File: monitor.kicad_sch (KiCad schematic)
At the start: 6 parts, among them K2 RT314A03, SW1 SW_Push, SW2 SW_Wuerth_450301014042, U2 LM397

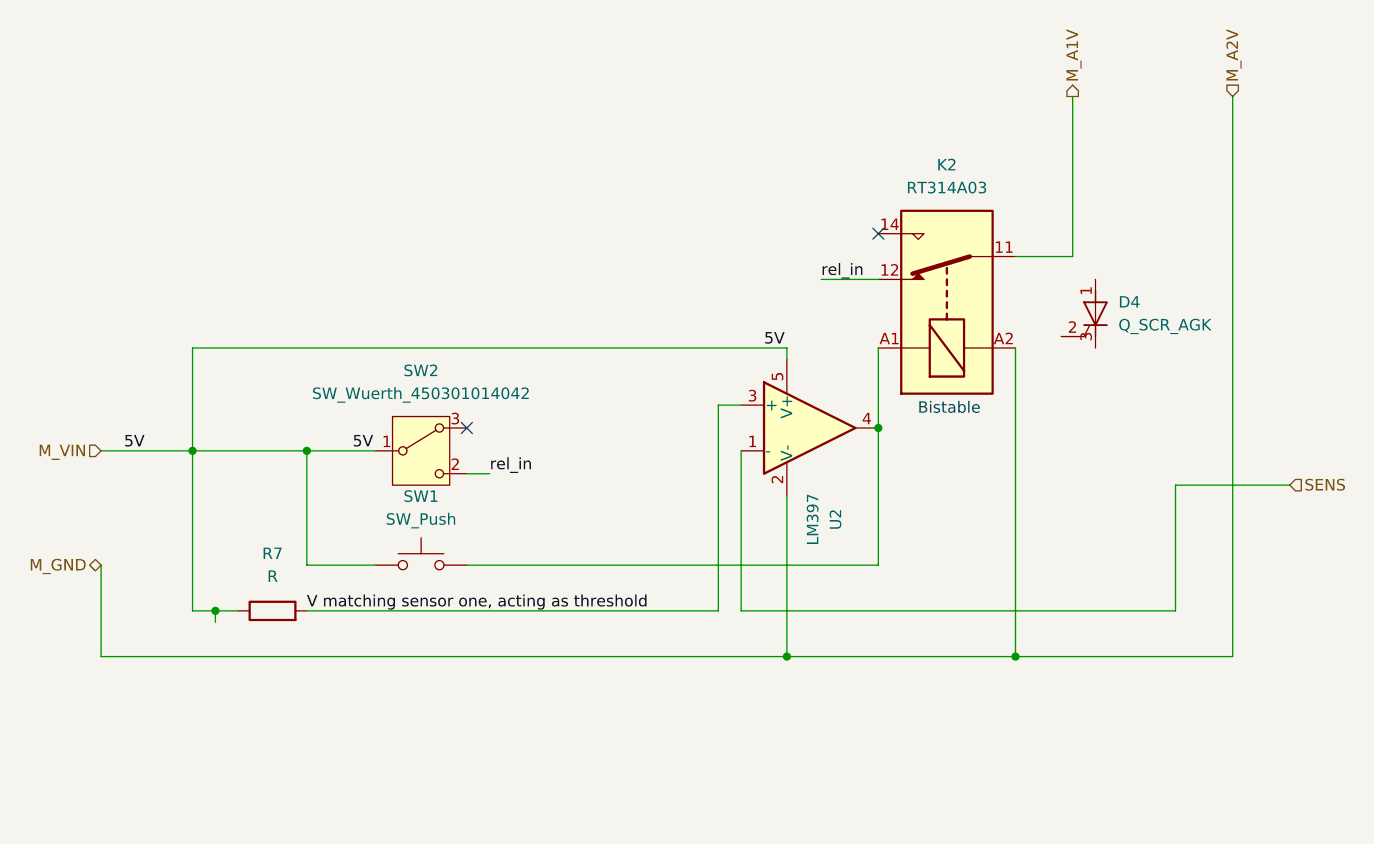
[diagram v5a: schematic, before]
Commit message: added scr instead of button
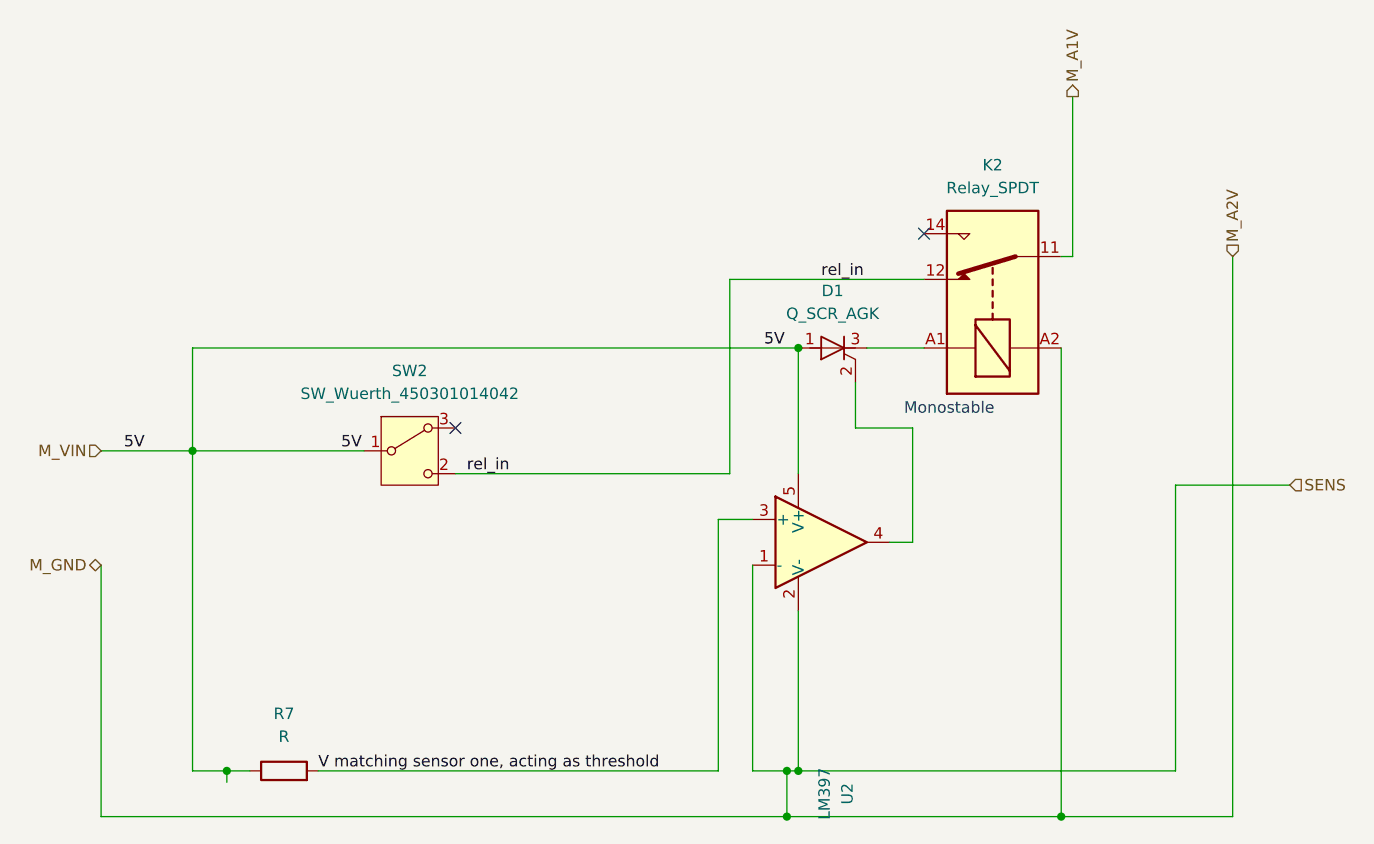
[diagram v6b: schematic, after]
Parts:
- removed D4: Q_SCR_AGK, symbol Device:Q_SCR_AGK
- removed K2: RT314A03, Relay_THT:Relay_SPDT_Schrack-RT1-16A-FormC_RM5mm, symbol Relay:RT314A05
- removed SW1: SW_Push, symbol Switch:SW_Push
- added D1: Q_SCR_AGK, symbol Device:Q_SCR_AGK
- added K2: Relay_SPDT, symbol Relay:Relay_SPDT
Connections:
- net SENS is gone; now on net M_A2V: U2.1 (-)
- net M_A1V: now also K2.11
- net M_A2V: now also K2.A2
- net M_VIN: now also D1.1 (A)
- net rel_in: now also K2.12
- net at U2.4: now also D1.2 (G)
- new net: D1.3 (K), K2.A1
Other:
- note added: "Monostable"
- note removed: "Bistable"
- moved on the sheet: R7, SW2, U2

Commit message: comparator wirirng
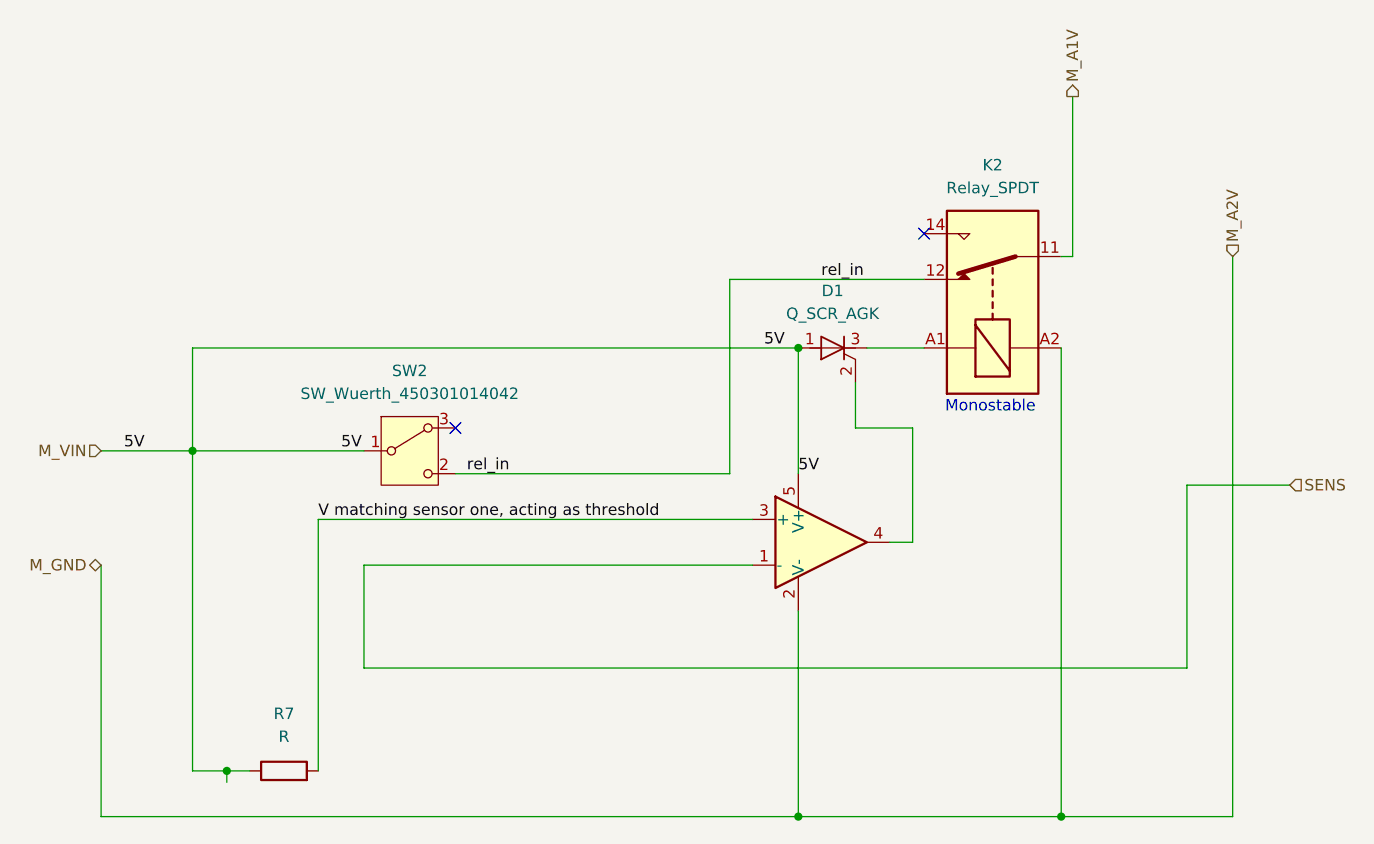
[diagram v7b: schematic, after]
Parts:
- K2: footprint (none) -> Relay_THT:Relay_SPDT_Finder_32.21-x000
- R7: footprint (none) -> Resistor_SMD:R_0201_0603Metric
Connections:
- net M_A2V: no longer U2.1 (-)
- new net SENS: U2.1 (-)
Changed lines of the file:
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@@
 	(text "Monostable"
 		(exclude_from_sim no)
-		(at 169.164 76.708 0)
+		(at 173.736 76.454 0)
 		(effects
 			(font
@@
 	)
 	(junction
-		(at 88.9 116.84)
+		(at 152.4 121.92)
 		(diameter 0)
 		(color 0 0 0 0)
 	)
 	(junction
-		(at 151.13 116.84)
+		(at 88.9 116.84)
 		(diameter 0)
 		(color 0 0 0 0)
@@
 	)
 	(junction
-		(at 152.4 116.84)
-		(diameter 0)
-		(color 0 0 0 0)
-	)
-	(junction
-		(at 151.13 121.92)
-		(diameter 0)
-		(color 0 0 0 0)
-	)
-	(junction
 		(at 85.09 81.28)
 		(diameter 0)
@@
 	(wire
 		(pts
-			(xy 151.13 116.84) (xy 147.32 116.84)
-		)
-		(stroke
-			(width 0)
-			(type default)
-		)
-	)
-	(wire
-		(pts
-			(xy 74.93 121.92) (xy 151.13 121.92)
-		)
-		(stroke
-			(width 0)
-			(type default)
-		)
-	)
-	(wire
-		(pts
-			(xy 143.51 88.9) (xy 143.51 116.84)
-		)
-		(stroke
-			(width 0)
-			(type default)
-		)
-	)
-	(wire
-		(pts
-			(xy 152.4 116.84) (xy 151.13 116.84)
+			(xy 74.93 121.92) (xy 152.4 121.92)
+		)
+		(stroke
+			(width 0)
+			(type default)
+		)
+	)
+	(wire
+		(pts
+			(xy 104.14 93.98) (xy 147.32 93.98)
 		)
 		(stroke
@@
 	(wire
 		(pts
+			(xy 99.06 88.9) (xy 99.06 116.84)
+		)
+		(stroke
+			(width 0)
+			(type default)
+		)
+	)
+	(wire
+		(pts
 			(xy 85.09 69.85) (xy 152.4 69.85)
 		)
@@
 	(wire
 		(pts
-			(xy 152.4 83.82) (xy 152.4 69.85)
+			(xy 152.4 69.85) (xy 152.4 83.82)
 		)
 		(stroke
@@
 	(wire
 		(pts
+			(xy 104.14 93.98) (xy 104.14 105.41)
+		)
+		(stroke
+			(width 0)
+			(type default)
+		)
+	)
+	(wire
+		(pts
 			(xy 144.78 62.23) (xy 166.37 62.23)
 		)
@@
 	(wire
 		(pts
+			(xy 152.4 121.92) (xy 181.61 121.92)
+		)
+		(stroke
+			(width 0)
+			(type default)
+		)
+	)
+	(wire
+		(pts
 			(xy 114.3 83.82) (xy 144.78 83.82)
 		)
@@
 	(wire
 		(pts
-			(xy 152.4 99.06) (xy 152.4 116.84)
+			(xy 152.4 99.06) (xy 152.4 121.92)
 		)
 		(stroke
@@
 	(wire
 		(pts
-			(xy 151.13 121.92) (xy 181.61 121.92)
-		)
-		(stroke
-			(width 0)
-			(type default)
-		)
-	)
-	(wire
-		(pts
 			(xy 200.66 121.92) (xy 200.66 59.69)
 		)
@@
 	(wire
 		(pts
-			(xy 147.32 116.84) (xy 147.32 93.98)
-		)
-		(stroke
-			(width 0)
-			(type default)
-		)
-	)
-	(wire
-		(pts
 			(xy 165.1 91.44) (xy 165.1 78.74)
 		)
@@
 	(wire
 		(pts
-			(xy 194.31 116.84) (xy 152.4 116.84)
-		)
-		(stroke
-			(width 0)
-			(type default)
-		)
-	)
-	(wire
-		(pts
-			(xy 151.13 116.84) (xy 151.13 121.92)
-		)
-		(stroke
-			(width 0)
-			(type default)
-		)
-	)
-	(wire
-		(pts
-			(xy 194.31 85.09) (xy 194.31 116.84)
-		)
-		(stroke
-			(width 0)
-			(type default)
-		)
-	)
-	(wire
-		(pts
-			(xy 207.01 85.09) (xy 194.31 85.09)
-		)
-		(stroke
-			(width 0)
-			(type default)
-		)
-	)
-	(wire
-		(pts
-			(xy 99.06 116.84) (xy 143.51 116.84)
+			(xy 104.14 105.41) (xy 195.58 105.41)
+		)
+		(stroke
+			(width 0)
+			(type default)
+		)
+	)
+	(wire
+		(pts
+			(xy 195.58 85.09) (xy 195.58 105.41)
+		)
+		(stroke
+			(width 0)
+			(type default)
+		)
+	)
+	(wire
+		(pts
+			(xy 207.01 85.09) (xy 195.58 85.09)
+		)
+		(stroke
+			(width 0)
+			(type default)
+		)
+	)
+	(wire
+		(pts
+			(xy 99.06 88.9) (xy 147.32 88.9)
 		)
 		(stroke
@@
 		(pts
 			(xy 181.61 121.92) (xy 200.66 121.92)
-		)
-		(stroke
-			(width 0)
-			(type default)
-		)
-	)
-	(wire
-		(pts
-			(xy 143.51 88.9) (xy 147.32 88.9)
 		)
 		(stroke
@@
 	)
 	(label "V matching sensor one, acting as threshold"
-		(at 99.06 116.84 0)
+		(at 99.06 88.9 0)
 		(effects
 			(font
@@
 	(label "5V"
 		(at 77.47 81.28 0)
+		(effects
+			(font
+				(size 1.27 1.27)
+			)
+			(justify left bottom)
+		)
+	)
+	(label "5V"
+		(at 152.4 83.82 0)
 		(effects
 			(font
@@
 					(size 1.27 1.27)
 				)
+				(hide yes)
 			)
 		)
@@
 					(size 1.27 1.27)
 				)
+				(hide yes)
 			)
 		)
@@
 			)
 		)
-		(property "Footprint" ""
+		(property "Footprint" "Relay_THT:Relay_SPDT_Finder_32.21-x000"
 			(at 175.26 53.34 0)
 			(effects
@@
 			)
 		)
-		(property "Footprint" ""
+		(property "Footprint" "Resistor_SMD:R_0201_0603Metric"
 			(at 95.25 118.618 90)
 			(effects

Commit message: added footprints
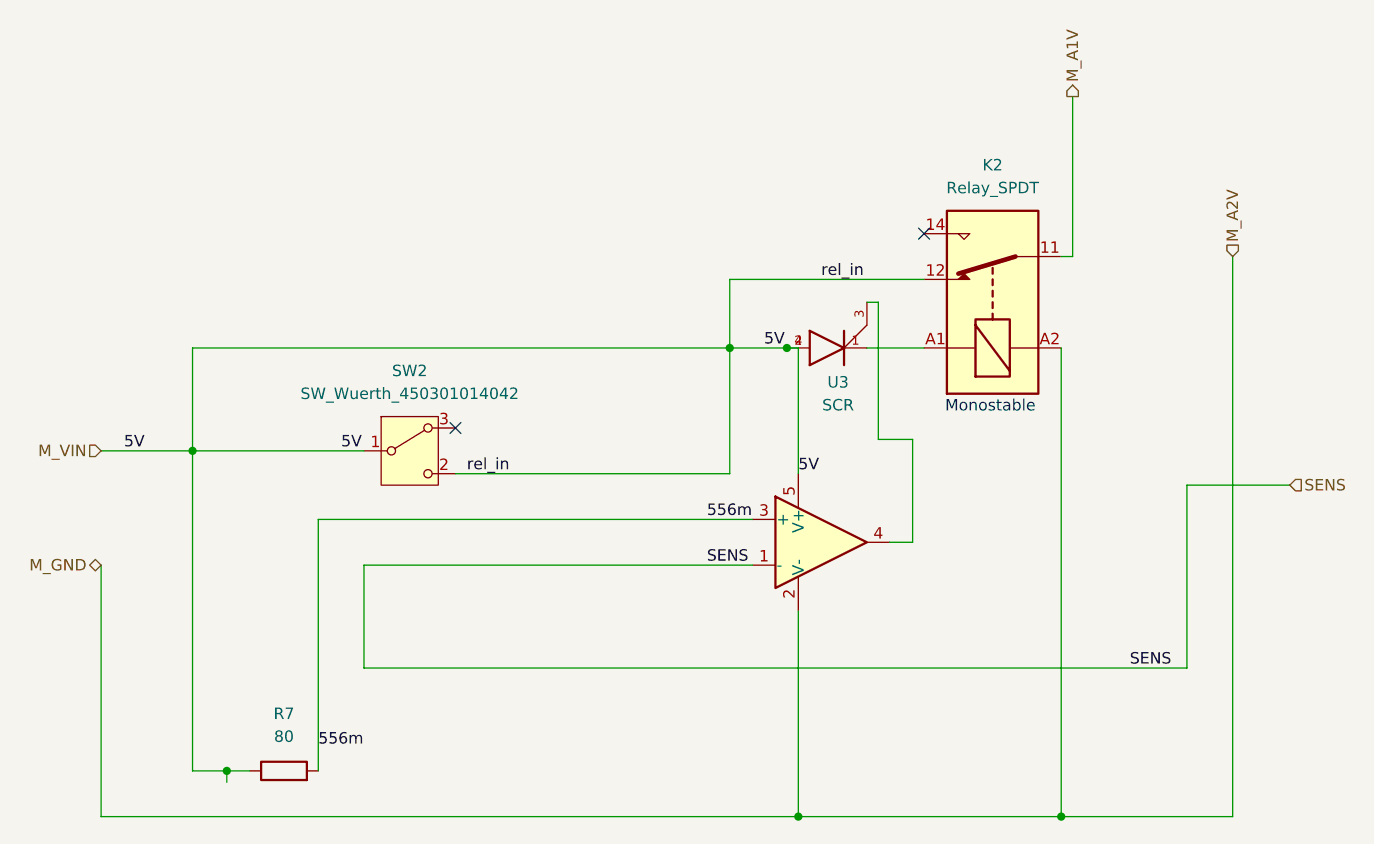
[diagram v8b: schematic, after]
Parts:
- removed D1: Q_SCR_AGK, symbol Device:Q_SCR_AGK
- added U3: SCR, SCR:SOT223, symbol SCR:SCR
- R7: value R -> 80
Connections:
- net rel_in is gone; now on net M_VIN: K2.12, SW2.2 (C)
- net M_VIN: now also U3.2, U3.4
- net at U2.4: now also U3.3
- net at K2.A1: now also U3.1
- net V matching sensor one, acting as threshold renamed 556m
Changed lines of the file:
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@@
 	)
 	(junction
-		(at 152.4 69.85)
+		(at 151.13 69.85)
+		(diameter 0)
+		(color 0 0 0 0)
+	)
+	(junction
+		(at 144.78 69.85)
 		(diameter 0)
 		(color 0 0 0 0)
@@
 	(wire
 		(pts
-			(xy 85.09 69.85) (xy 152.4 69.85)
+			(xy 85.09 69.85) (xy 144.78 69.85)
 		)
 		(stroke
@@
 	(wire
 		(pts
-			(xy 165.1 78.74) (xy 158.75 78.74)
+			(xy 165.1 80.01) (xy 161.29 80.01)
 		)
 		(stroke
@@
 	(wire
 		(pts
+			(xy 144.78 69.85) (xy 144.78 83.82)
+		)
+		(stroke
+			(width 0)
+			(type default)
+		)
+	)
+	(wire
+		(pts
 			(xy 181.61 69.85) (xy 181.61 121.92)
 		)
@@
 	(wire
 		(pts
+			(xy 151.13 69.85) (xy 144.78 69.85)
+		)
+		(stroke
+			(width 0)
+			(type default)
+		)
+	)
+	(wire
+		(pts
 			(xy 200.66 121.92) (xy 200.66 59.69)
 		)
@@
 	(wire
 		(pts
-			(xy 165.1 91.44) (xy 165.1 78.74)
+			(xy 165.1 91.44) (xy 165.1 80.01)
 		)
 		(stroke
@@
 	(wire
 		(pts
+			(xy 161.29 64.77) (xy 160.02 64.77)
+		)
+		(stroke
+			(width 0)
+			(type default)
+		)
+	)
+	(wire
+		(pts
 			(xy 88.9 118.11) (xy 88.9 116.84)
 		)
@@
 	(wire
 		(pts
-			(xy 158.75 78.74) (xy 158.75 73.66)
-		)
-		(stroke
-			(width 0)
-			(type default)
-		)
-	)
-	(wire
-		(pts
-			(xy 144.78 83.82) (xy 144.78 62.23)
+			(xy 161.29 64.77) (xy 161.29 80.01)
+		)
+		(stroke
+			(width 0)
+			(type default)
+		)
+	)
+	(wire
+		(pts
+			(xy 144.78 62.23) (xy 144.78 69.85)
 		)
 		(stroke
@@
 		(pts
 			(xy 181.61 121.92) (xy 200.66 121.92)
+		)
+		(stroke
+			(width 0)
+			(type default)
+		)
+	)
+	(wire
+		(pts
+			(xy 151.13 69.85) (xy 152.4 69.85)
 		)
 		(stroke
@@
 		)
 	)
+	(label "556m"
+		(at 99.06 114.3 0)
+		(effects
+			(font
+				(size 1.27 1.27)
+			)
+			(justify left bottom)
+		)
+	)
+	(label "SENS"
+		(at 189.23 105.41 0)
+		(effects
+			(font
+				(size 1.27 1.27)
+			)
+			(justify left bottom)
+		)
+	)
+	(label "556m"
+		(at 142.24 88.9 0)
+		(effects
+			(font
+				(size 1.27 1.27)
+			)
+			(justify left bottom)
+		)
+	)
 	(label "rel_in"
 		(at 154.94 62.23 0)
@@
 		)
 	)
-	(label "V matching sensor one, acting as threshold"
-		(at 99.06 88.9 0)
+	(label "SENS"
+		(at 142.24 93.98 0)
 		(effects
 			(font
@@
 	)
 	(symbol
-		(lib_id "Device:Q_SCR_AGK")
-		(at 156.21 69.85 90)
+		(lib_id "SCR:SCR")
+		(at 154.94 69.85 270)
 		(unit 1)
 		(exclude_from_sim no)
@@
 		(dnp no)
 		(fields_autoplaced yes)
-		(property "Reference" "D1"
-			(at 156.21 63.5 90)
-			(effects
-				(font
-					(size 1.27 1.27)
-				)
-			)
-		)
-		(property "Value" "Q_SCR_AGK"
-			(at 156.21 66.04 90)
-			(effects
-				(font
-					(size 1.27 1.27)
-				)
-			)
-		)
-		(property "Footprint" ""
-			(at 156.21 69.85 90)
-			(effects
-				(font
-					(size 1.27 1.27)
-				)
-				(hide yes)
-			)
-		)
-		(property "Datasheet" "~"
-			(at 156.21 69.85 90)
-			(effects
-				(font
-					(size 1.27 1.27)
-				)
-				(hide yes)
-			)
-		)
-		(property "Description" "Silicon controlled rectifier, anode/gate/cathode"
-			(at 156.21 69.85 0)
-			(effects
-				(font
-					(size 1.27 1.27)
-				)
-				(hide yes)
-			)
+		(property "Reference" "U3"
+			(at 156.819 73.66 90)
+			(effects
+				(font
+					(size 1.27 1.27)
+				)
+			)
+		)
+		(property "Value" "SCR"
+			(at 156.819 76.2 90)
+			(effects
+				(font
+					(size 1.27 1.27)
+				)
+			)
+		)
+		(property "Footprint" "SCR:SOT223"
+			(at 154.94 69.85 0)
+			(effects
+				(font
+					(size 1.27 1.27)
+				)
+				(justify bottom)
+				(hide yes)
+			)
+		)
+		(property "Datasheet" ""
+			(at 154.94 69.85 0)
+			(effects
+				(font
+					(size 1.27 1.27)
+				)
+				(hide yes)
+			)
+		)
+		(property "Description" ""
+			(at 154.94 69.85 0)
+			(effects
+				(font
+					(size 1.27 1.27)
+				)
+				(hide yes)
+			)
+		)
+		(property "MF" "EPC"
+			(at 154.94 69.85 0)
+			(effects
+				(font
+					(size 1.27 1.27)
+				)
+				(justify bottom)
+				(hide yes)
+			)
+		)
+		(property "Description_1" "Bipolar (BJT) Transistor NPN 40V 200mA 300MHz 300mW Surface Mount SOT-23-3"
+			(at 154.94 69.85 0)
+			(effects
+				(font
+					(size 1.27 1.27)
+				)
+				(justify bottom)
+				(hide yes)
+			)
+		)
+		(property "Package" "None"
+			(at 154.94 69.85 0)
+			(effects
+				(font
+					(size 1.27 1.27)
+				)
+				(justify bottom)
+				(hide yes)
+			)
+		)
+		(property "Price" "None"
+			(at 154.94 69.85 0)
+			(effects
+				(font
+					(size 1.27 1.27)
+				)
+				(justify bottom)
+				(hide yes)
+			)
+		)
+		(property "SnapEDA_Link" "https://www.snapeda.com/parts/SCR/EPC/view-part/?ref=snap"
+			(at 154.94 69.85 0)
+			(effects
+				(font
+					(size 1.27 1.27)
+				)
+				(justify bottom)
+				(hide yes)
+			)
+		)
+		(property "MP" "SCR"
+			(at 154.94 69.85 0)
+			(effects
+				(font
+					(size 1.27 1.27)
+				)
+				(justify bottom)
+				(hide yes)
+			)
+		)
+		(property "Availability" "Not in stock"
+			(at 154.94 69.85 0)
+			(effects
+				(font
+					(size 1.27 1.27)
+				)
+				(justify bottom)
+				(hide yes)
+			)
+		)
+		(property "Check_prices" "https://www.snapeda.com/parts/SCR/EPC/view-part/?ref=eda"
+			(at 154.94 69.85 0)
+			(effects
+				(font
+					(size 1.27 1.27)
+				)
+				(justify bottom)
+				(hide yes)
+			)
+		)
+		(pin "1"
+		)
+		(pin "3"
 		)
 		(pin "2"
 		)
-		(pin "1"
-		)
-		(pin "3"
+		(pin "4"
 		)
 		(instances
-			(project "recruitment"
+			(project ""
 				(path "/bdc7face-9f7c-4701-80bb-4cc144448db1/10220f6e-30e0-4da2-bc7c-0672de199a7a"
-					(reference "D1")
+					(reference "U3")
 					(unit 1)
 				)
@@
 			)
 		)
-		(property "Value" "R"
+		(property "Value" "80"
 			(at 95.25 113.03 90)
 			(effects
